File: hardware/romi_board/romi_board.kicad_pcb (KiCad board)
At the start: 2 copper layers, 93.2 x 62.7 mm, 1 part, among them U1 Teensy4.0

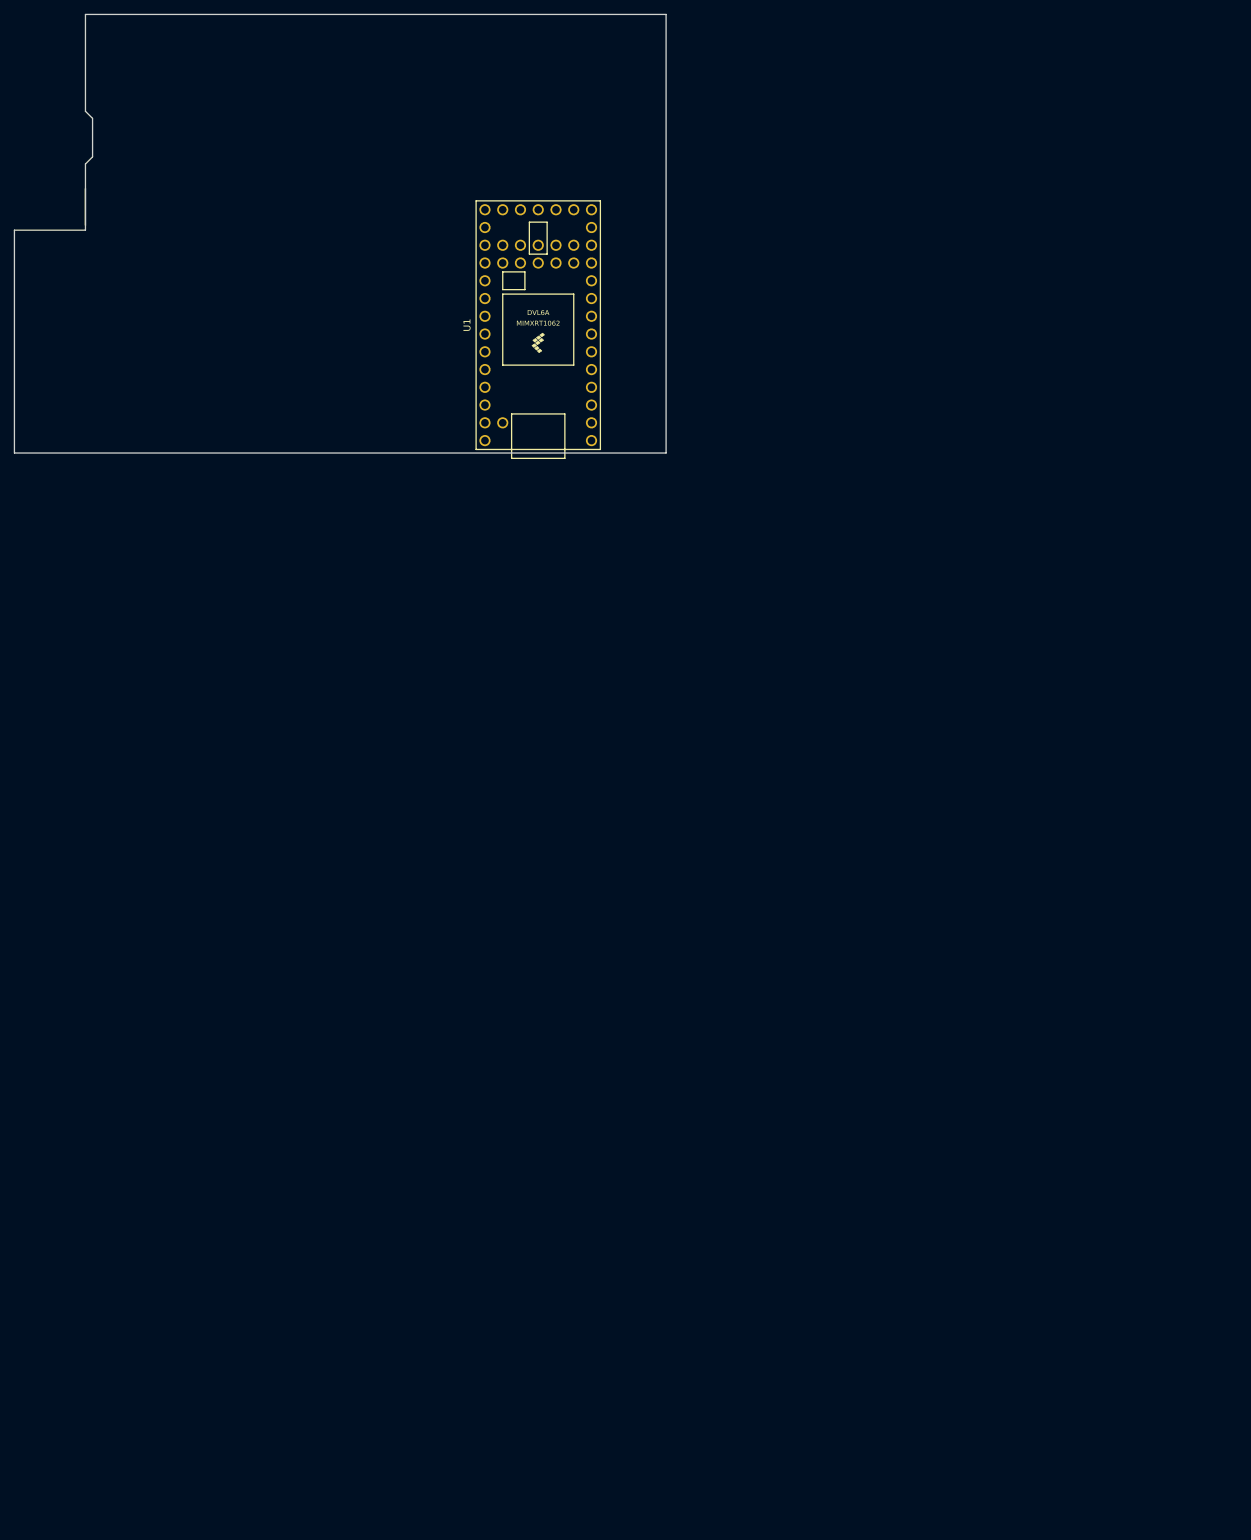
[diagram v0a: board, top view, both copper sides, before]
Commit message: Roll back to KiCAD v5.1.2 and add project specific libraries
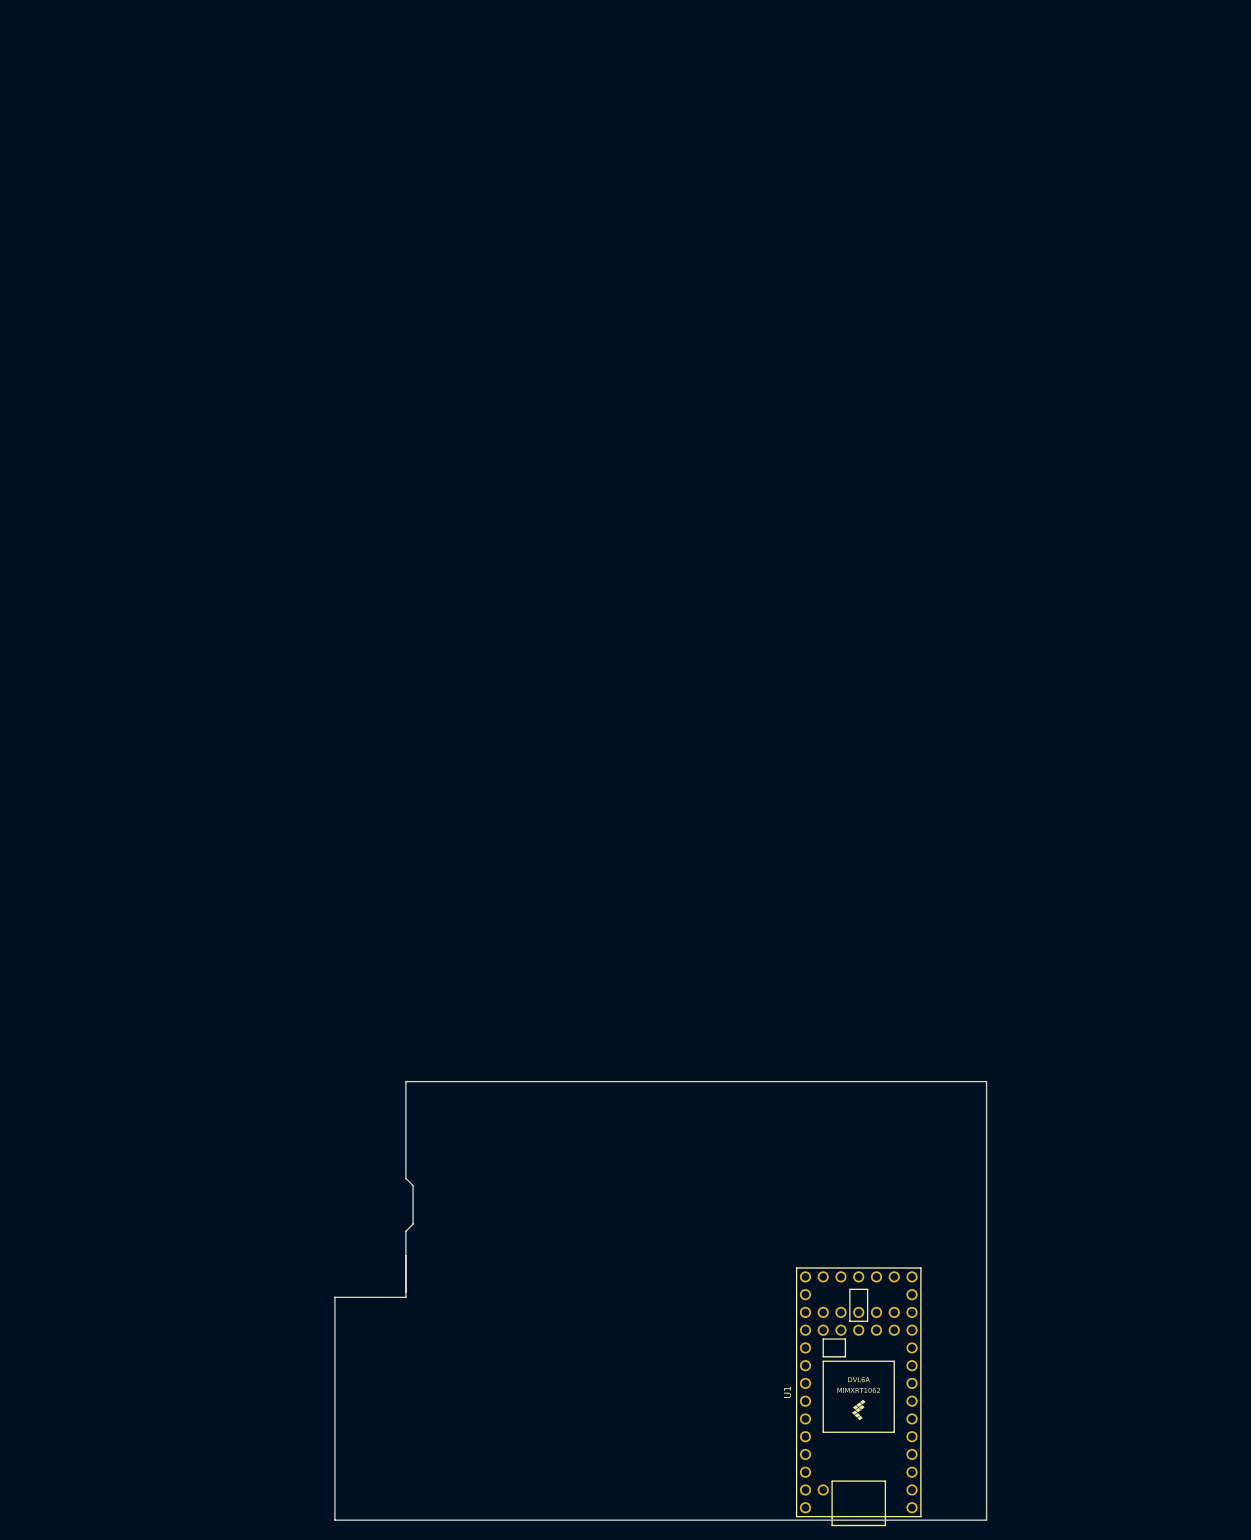
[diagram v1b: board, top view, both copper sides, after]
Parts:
- moved U1 159.4 mm to (120.8, 134.4)

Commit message: Delete Pololu board outline and add rough PART dxf board outlines
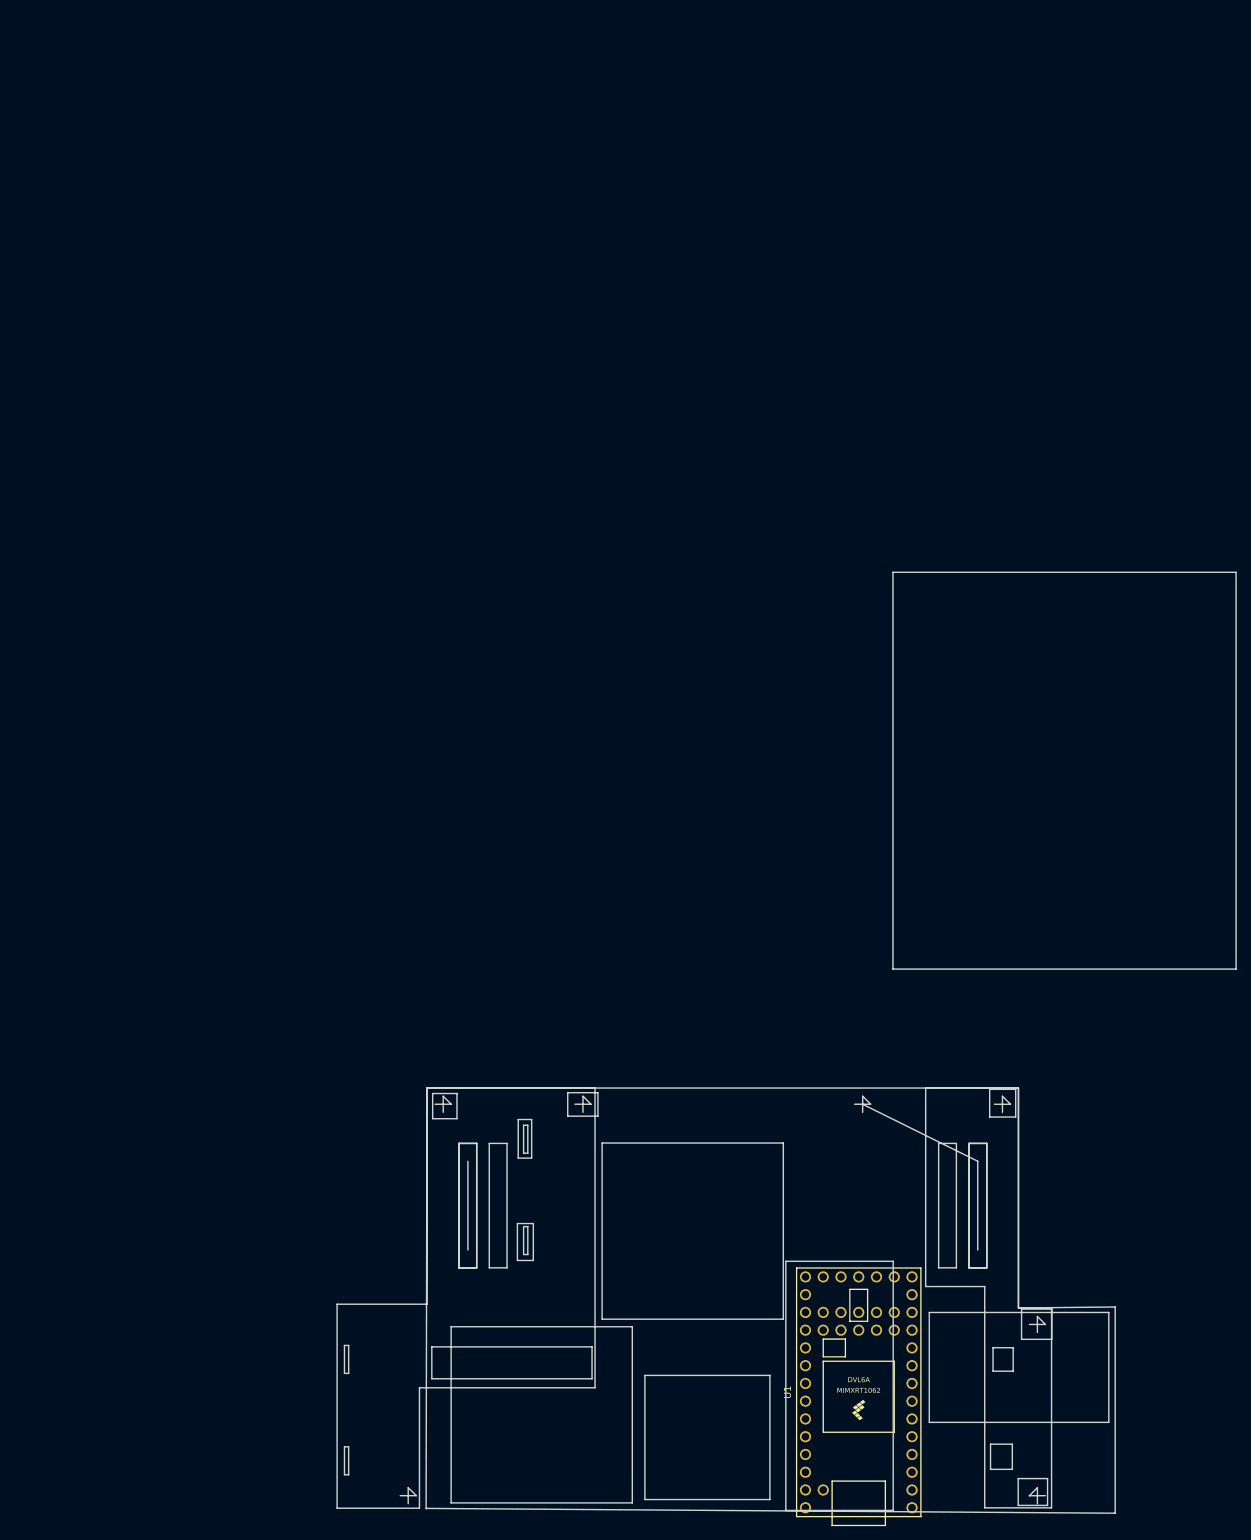
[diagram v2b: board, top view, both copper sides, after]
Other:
- board size 93.2 x 62.7 mm -> 128.6 x 134.6 mm
